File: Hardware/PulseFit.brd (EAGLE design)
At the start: 51.5 x 56.1 mm, 49 parts, among them SW1 SWITCH.JS202011JCQN

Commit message: first itteration of pulsefit
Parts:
- moved C12 131.3 mm to (66.4, 8.31), flipped to the bottom
- moved C11 124.4 mm to (72.3, 2.31), flipped to the bottom
- moved AMP 116.4 mm to (60.0, 29.9), flipped to the bottom, turned to 90 degrees
- moved D1 114.0 mm to (61.5, 34.9), flipped to the bottom
- moved C3 106.8 mm to (61.0, 2.31), flipped to the bottom
- moved R4 102.7 mm to (59.2, 33.2), flipped to the bottom, turned to 180 degrees
- moved R5 100.7 mm to (59.1, 35.8), flipped to the bottom
- moved R8 89.0 mm to (55.6, 35.3), flipped to the bottom
- moved R13 88.7 mm to (54.3, 33.6), flipped to the bottom
- moved PD 87.1 mm to (51.3, 28.9), turned to 180.5 degrees
- moved R6 86.6 mm to (51.8, 37.3), flipped to the bottom
- moved R9 86.1 mm to (56.4, 33.6), flipped to the bottom
- moved C9 84.8 mm to (48.7, 38.6), flipped to the bottom
- moved C6 84.2 mm to (51.8, 38.6), flipped to the bottom
- moved C8 84.1 mm to (48.8, 36.0), flipped to the bottom
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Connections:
- net PEAK: now also BREAKOUT.3; no longer BREAKOUT.2
- net PULSE: now also BREAKOUT.2; no longer BREAKOUT.3
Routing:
- net PEAK: track 17.5 -> 49.3 mm, vias 0 -> 1
- net N$14: track 0.00 -> 27.2 mm
- net N$15: track 0.00 -> 23.6 mm
- net COMP: track 19.6 -> 41.7 mm
- net GND: track 0.00 -> 18.9 mm, vias 0 -> 6
- net PULSE: track 32.6 -> 51.1 mm, vias 2 -> 1
- net N$17: track 0.00 -> 18.4 mm
- net N$5: track 0.00 -> 14.2 mm, vias 0 -> 1
- net 3.3V: track 1.20 -> 13.1 mm, vias 1 -> 9
- net N$18: track 0.00 -> 9.55 mm, vias 0 -> 1
- net N$1: track 0.00 -> 7.79 mm
- net N$4: track 0.00 -> 7.66 mm
- net N$10: track 0.00 -> 2.84 mm
- net N$3: track 0.00 -> 2.84 mm
- net ANODE: track 145.5 -> 148.3 mm
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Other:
- board size 51.5 x 56.1 mm -> 53.2 x 56.2 mm

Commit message: next board
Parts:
- moved C8 17.8 mm to (64.8, 28.3), turned to 270 degrees
- moved C2 16.6 mm to (60.2, 22.0)
- moved C7 16.1 mm to (61.6, 27.5), turned to 180 degrees
- moved C9 15.7 mm to (61.6, 29.7), turned to 180 degrees
- moved R2 12.9 mm to (53.6, 33.4)
- moved R6 12.3 mm to (58.2, 26.8), turned to 90 degrees
- moved C6 11.1 mm to (58.4, 29.7), turned to 180 degrees
- moved R4 10.4 mm to (59.9, 43.6), turned to 0 degrees
- moved LED1 9.53 mm to (51.0, 35.4), turned to 0.2 degrees
- moved PD 8.95 mm to (51.0, 37.8)
- moved C10 8.05 mm to (64.7, 43.4), turned to 90 degrees
- moved D1 8.03 mm to (62.2, 42.9)
- moved R12 8.00 mm to (64.4, 31.7), turned to 270 degrees
- moved AMP 7.63 mm to (63.0, 37.0)
- moved R3 7.51 mm to (62.2, 32.1)
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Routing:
- net N$14: track 27.2 -> 5.81 mm
- net GND: track 18.9 -> 3.68 mm, vias 6 -> 2
- net PULSE: track 51.1 -> 36.2 mm, vias 1 -> 2
- net N$15: track 23.6 -> 8.75 mm
- net N$18: track 9.55 -> 23.9 mm
- net PEAK: track 49.3 -> 38.0 mm, vias 1 -> 3
- net N$17: track 18.4 -> 11.8 mm
- net N$10: track 2.84 -> 6.22 mm
- net 3.3V: track 13.1 -> 16.0 mm
- net ANODE: track 148.3 -> 145.5 mm
- net N$13: track 2.56 -> 4.72 mm
- net N$9: track 3.61 -> 4.92 mm
- net COMP: track 41.7 -> 40.4 mm, vias 0 -> 3
- net N$3: track 2.84 -> 3.68 mm
- net N$4: track 7.66 -> 7.13 mm
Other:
- board size 53.2 x 56.2 mm -> 52.3 x 56.2 mm

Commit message: deleted extra bypass capacitors and changed their values a bit
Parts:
- removed C3, C4: 2.2u, CalvEngIO-Passives:C0603
- C1, C2: value 100n -> 1u
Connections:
- net 3.3V: no longer C3.2, C4.2
- net GND: no longer C3.1, C4.1
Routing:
- net 3.3V: track 16.0 -> 12.6 mm, vias 9 -> 7
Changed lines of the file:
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@@
 <?xml version="1.0" encoding="utf-8"?>
 <!DOCTYPE eagle SYSTEM "eagle.dtd">
-<eagle version="8.0.0">
+<eagle version="8.2.2">
 <drawing>
 <settings>
@@
 <attribute name="VALUE" x="62.8396" y="42.799" size="1.27" layer="28" rot="MR90"/>
 </element>
-<element name="C2" library="CalvEngIO-Passives" package="C0402" value="100n" x="60.2488" y="22.0218" smashed="yes" rot="MR0">
+<element name="C2" library="CalvEngIO-Passives" package="C0402" value="1u" x="60.2488" y="22.0218" smashed="yes" rot="MR0">
 <attribute name="NAME" x="59.817" y="23.2664" size="0.6096" layer="26" rot="MR180"/>
 <attribute name="VALUE" x="60.8838" y="20.1168" size="1.27" layer="28" rot="MR0"/>
@@
 <attribute name="VALUE" x="56.261" y="26.2128" size="1.27" layer="28" rot="MR90"/>
 </element>
-<element name="C1" library="CalvEngIO-Passives" package="C0402" value="100n" x="60.198" y="24.2316" smashed="yes" rot="MR0">
+<element name="C1" library="CalvEngIO-Passives" package="C0402" value="1u" x="60.198" y="24.2316" smashed="yes" rot="MR0">
 <attribute name="NAME" x="60.198" y="25.146" size="0.6096" layer="26" rot="MR0"/>
 <attribute name="VALUE" x="60.833" y="22.3266" size="1.27" layer="28" rot="MR0"/>
@@
 <attribute name="NAME" x="61.9252" y="34.2392" size="0.6096" layer="26" ratio="10" rot="MR180"/>
 <attribute name="VALUE" x="60.9092" y="40.8686" size="1.016" layer="28" ratio="10" rot="MR180"/>
-</element>
-<element name="C3" library="CalvEngIO-Passives" package="C0603" value="2.2u" x="62.7634" y="6.9596" smashed="yes" rot="MR0">
-<attribute name="NAME" x="63.1444" y="8.0264" size="0.6096" layer="26" rot="MR0"/>
-<attribute name="VALUE" x="63.3984" y="5.0546" size="1.27" layer="28" rot="MR0"/>
-</element>
-<element name="C4" library="CalvEngIO-Passives" package="C0603" value="2.2u" x="62.7634" y="4.445" smashed="yes" rot="MR0">
-<attribute name="NAME" x="63.2206" y="3.0988" size="0.6096" layer="26" rot="MR0"/>
-<attribute name="VALUE" x="63.3984" y="2.54" size="1.27" layer="28" rot="MR0"/>
 </element>
 <element name="U$6" library="CalvEngIO-Power" package="SOT23-5" value="AP2210-ADJ" x="62.7126" y="10.7188" smashed="yes" rot="MR180">
@@
 <contactref element="C5" pad="2"/>
 <contactref element="AMP" pad="11"/>
-<contactref element="C3" pad="1"/>
-<contactref element="C4" pad="1"/>
 <contactref element="U$6" pad="2"/>
 <contactref element="C11" pad="2"/>
@@
 <wire x1="70.1642" y1="21.1742" x2="68.3768" y2="22.9616" width="0.3048" layer="1"/>
 <via x="68.3768" y="22.9616" extent="1-16" drill="0.4064"/>
+<wire x1="64.7446" y1="42.484" x2="70.2818" y2="43.7642" width="0" layer="19" extent="16-16"/>
+<wire x1="63.7032" y1="47.0154" x2="64.7446" y2="42.484" width="0" layer="19" extent="16-16"/>
+<wire x1="59.2432" y1="41.8084" x2="64.7446" y2="42.484" width="0" layer="19" extent="16-16"/>
+<wire x1="56.6928" y1="45.847" x2="59.2432" y2="41.8084" width="0" layer="19" extent="16-16"/>
+<wire x1="65.7098" y1="36.9824" x2="64.7446" y2="42.484" width="0" layer="19" extent="16-16"/>
+<wire x1="71.12" y1="37.8206" x2="65.7098" y2="36.9824" width="0" layer="19" extent="16-16"/>
+<wire x1="64.4398" y1="31.0238" x2="65.7098" y2="36.9824" width="0" layer="19" extent="16-16"/>
+<wire x1="64.8462" y1="29.171" x2="64.4398" y2="31.0238" width="0" layer="19" extent="16-16"/>
+<wire x1="67.564" y1="30.0736" x2="64.8462" y2="29.171" width="0" layer="19" extent="16-16"/>
+<wire x1="60.848" y1="24.2316" x2="64.8462" y2="29.171" width="0" layer="19" extent="16-16"/>
+<wire x1="60.8988" y1="22.0218" x2="60.848" y2="24.2316" width="0" layer="19" extent="16-16"/>
+<wire x1="62.865" y1="23.0886" x2="60.8988" y2="22.0218" width="0" layer="19" extent="16-16"/>
+<wire x1="58.166" y1="26.1978" x2="60.848" y2="24.2316" width="0" layer="19" extent="16-16"/>
+<wire x1="68.3768" y1="22.9616" x2="62.865" y2="23.0886" width="0" layer="19" extent="1-1"/>
+<wire x1="58.8772" y1="16.256" x2="60.8988" y2="22.0218" width="0" layer="19" extent="16-16"/>
+<wire x1="62.7126" y1="12.0248" x2="58.8772" y2="16.256" width="0" layer="19" extent="16-16"/>
+<wire x1="65.698" y1="14.8336" x2="62.7126" y2="12.0248" width="0" layer="19" extent="16-16"/>
+<wire x1="67.0964" y1="11.5062" x2="65.698" y2="14.8336" width="0" layer="19" extent="16-16"/>
+<wire x1="65.571" y1="6.1976" x2="67.0964" y2="11.5062" width="0" layer="19" extent="16-16"/>
+<wire x1="54.7474" y1="31.2928" x2="58.166" y2="26.1978" width="0" layer="19" extent="16-16"/>
+<wire x1="53.5686" y1="32.7002" x2="54.7474" y2="31.2928" width="0" layer="19" extent="16-16"/>
+<wire x1="51.597503125" y1="38.501209375" x2="53.5686" y2="32.7002" width="0" layer="19" extent="1-16"/>
+<wire x1="50.8508" y1="41.656" x2="51.597503125" y2="39.461496875" width="0" layer="19" extent="1-1"/>
+<wire x1="44.7802" y1="45.8216" x2="50.8508" y2="41.656" width="0" layer="19" extent="1-1"/>
+<wire x1="37.5666" y1="46.6344" x2="44.7802" y2="45.8216" width="0" layer="19" extent="1-1"/>
+<wire x1="33.0454" y1="43.8404" x2="37.5666" y2="46.6344" width="0" layer="19" extent="1-1"/>
+<wire x1="31.1404" y1="36.6014" x2="33.0454" y2="43.8404" width="0" layer="19" extent="1-1"/>
+<wire x1="54.6354" y1="9.6266" x2="58.8772" y2="16.256" width="0" layer="19" extent="1-1"/>
+<wire x1="50.4952" y1="5.2578" x2="54.6354" y2="9.6266" width="0" layer="19" extent="1-1"/>
+<wire x1="46.736" y1="9.4488" x2="50.4952" y2="5.2578" width="0" layer="19" extent="1-1"/>
+<wire x1="42.7736" y1="15.7734" x2="46.736" y2="9.4488" width="0" layer="19" extent="1-1"/>
+<wire x1="38.5318" y1="22.2758" x2="42.7736" y2="15.7734" width="0" layer="19" extent="1-1"/>
+<wire x1="34.3916" y1="29.1338" x2="38.5318" y2="22.2758" width="0" layer="19" extent="1-1"/>
+<wire x1="53.3146" y1="54.61" x2="56.6928" y2="45.847" width="0" layer="19" extent="1-1"/>
 </signal>
 <signal name="PULSE">
@@
 <contactref element="C2" pad="2"/>
 <contactref element="AMP" pad="4"/>
-<contactref element="C3" pad="2"/>
 <contactref element="R4" pad="2"/>
 <contactref element="LED1" pad="+"/>
 <contactref element="PD" pad="1"/>
 <contactref element="C1" pad="2"/>
-<contactref element="C4" pad="2"/>
 <polygon width="0.2032" layer="1">
 <vertex x="23.4188" y="56.0324"/>
@@
 <wire x1="60.4118" y1="9.4128" x2="60.3758" y2="9.4488" width="0.3048" layer="16"/>
 <via x="60.3758" y="9.4488" extent="1-16" drill="0.4064"/>
-<wire x1="61.9134" y1="6.9596" x2="60.2488" y2="6.9596" width="0.3048" layer="16"/>
-<via x="60.2488" y="6.9596" extent="1-16" drill="0.4064"/>
-<wire x1="61.9134" y1="4.445" x2="60.3758" y2="4.445" width="0.3048" layer="16"/>
-<wire x1="60.3758" y1="4.445" x2="60.2488" y2="4.572" width="0.3048" layer="16"/>
-<via x="60.2488" y="4.572" extent="1-16" drill="0.4064"/>
 <wire x1="67.271" y1="6.1976" x2="67.2592" y2="4.445" width="0.3048" layer="16"/>
 <via x="67.2592" y="4.445" extent="1-16" drill="0.4064"/>
+<wire x1="57.6072" y1="43.5356" x2="55.8546" y2="54.61" width="0" layer="19" extent="16-16"/>
+<wire x1="57.1754" y1="36.9824" x2="57.6072" y2="43.5356" width="0" layer="19" extent="16-16"/>
+<wire x1="50.40889375" y1="37.1907875" x2="57.15" y2="36.957" width="0" layer="19" extent="1-16"/>
 <wire x1="48.5004125" y1="35.426784375" x2="50.40889375" y2="37.1907875" width="0" layer="19" extent="1-1"/>
+<wire x1="53.2892" y1="29.7688" x2="48.5004125" y2="35.426784375" width="0" layer="19" extent="1-16"/>
+<wire x1="57.8866" y1="24.2316" x2="54.7728" y2="29.718" width="0" layer="19" extent="16-16"/>
+<wire x1="58.0898" y1="22.098" x2="57.8866" y2="24.2316" width="0" layer="19" extent="16-16"/>
+<wire x1="60.3758" y1="9.4488" x2="59.5988" y2="22.0218" width="0" layer="19" extent="16-16"/>
+<wire x1="67.271" y1="6.1976" x2="61.7626" y2="9.4128" width="0" layer="19" extent="16-16"/>
 </signal>
 <signal name="N$3">

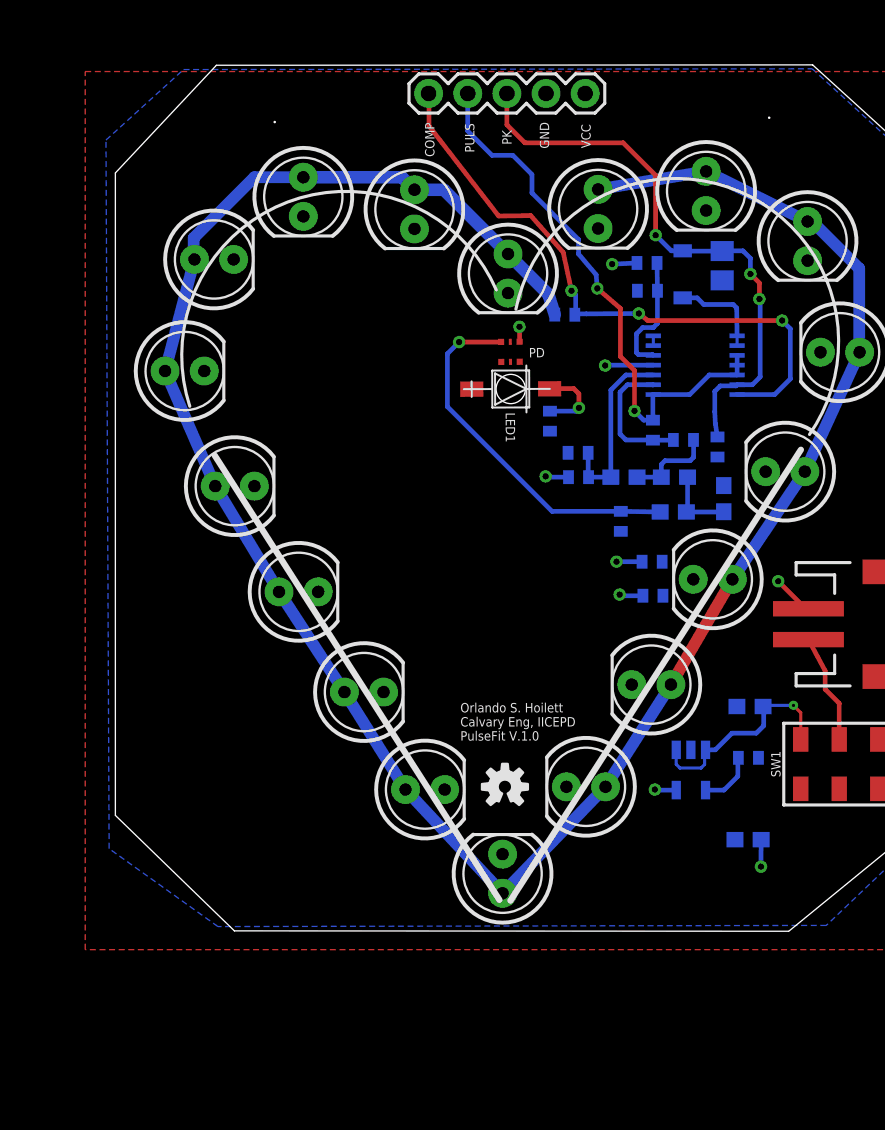
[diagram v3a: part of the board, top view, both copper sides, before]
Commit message: slight updates moving capacitors around and such
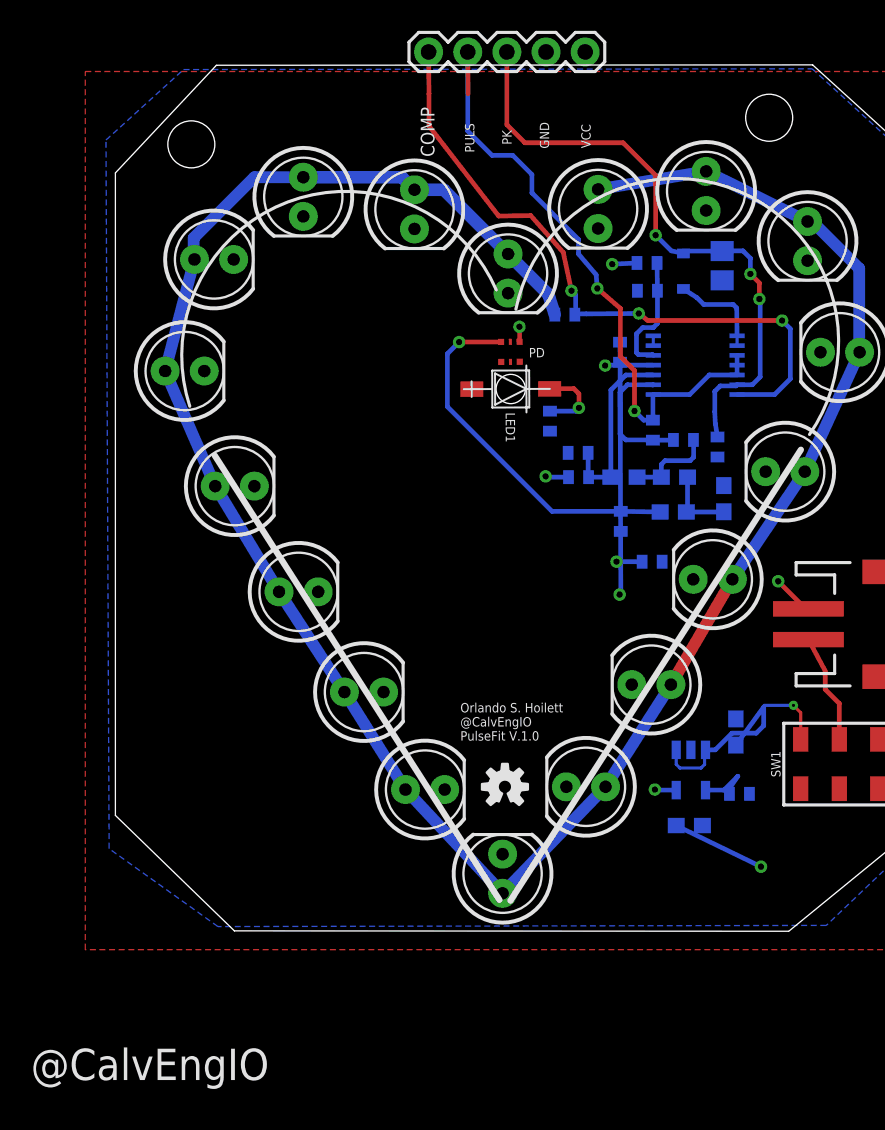
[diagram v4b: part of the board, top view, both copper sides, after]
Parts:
- added U$1: CALVENGIO_HANDLEHANDLE.08, CalvEngIO-Logos:CALVENGIO_HANDLE.08
- D1: device CalvEngIO-DiscreteSemi:SOD123 -> CalvEngIO-DiscreteSemi:SOD-323
- moved C2 15.9 mm to (58.1, 37.8), turned to 90 degrees
- moved C11 3.92 mm to (62.6, 7.11), turned to 180 degrees
- moved BREAKOUT 2.69 mm to (45.7, 57.3)
- moved C12 2.41 mm to (65.9, 9.17)
- moved C5 1.89 mm to (65.6, 13.2), turned to 90 degrees
- moved D1 0.21 mm to (62.2, 43.1), turned to 270 degrees
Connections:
- net N$10: now also D1.A; no longer D1.ANODE
- net PEAK: now also D1.C; no longer D1.CATH
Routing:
- net 3.3V: track 12.6 -> 32.0 mm
- net N$5: track 14.0 -> 20.1 mm
- net PULSE: track 36.2 -> 41.6 mm
- net PEAK: track 38.0 -> 40.9 mm
- net COMP: track 40.4 -> 43.1 mm
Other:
- board text added: "Orlando S. Hoilett @CalvEngIO PulseFit V.1.0"
- board text removed: "Orlando S. Hoilett Calvary Eng, IICEPD PulseFit V.1.0"
